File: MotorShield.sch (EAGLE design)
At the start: 88 parts, among them IC1 OPA4340E, IC2 OPA4340E

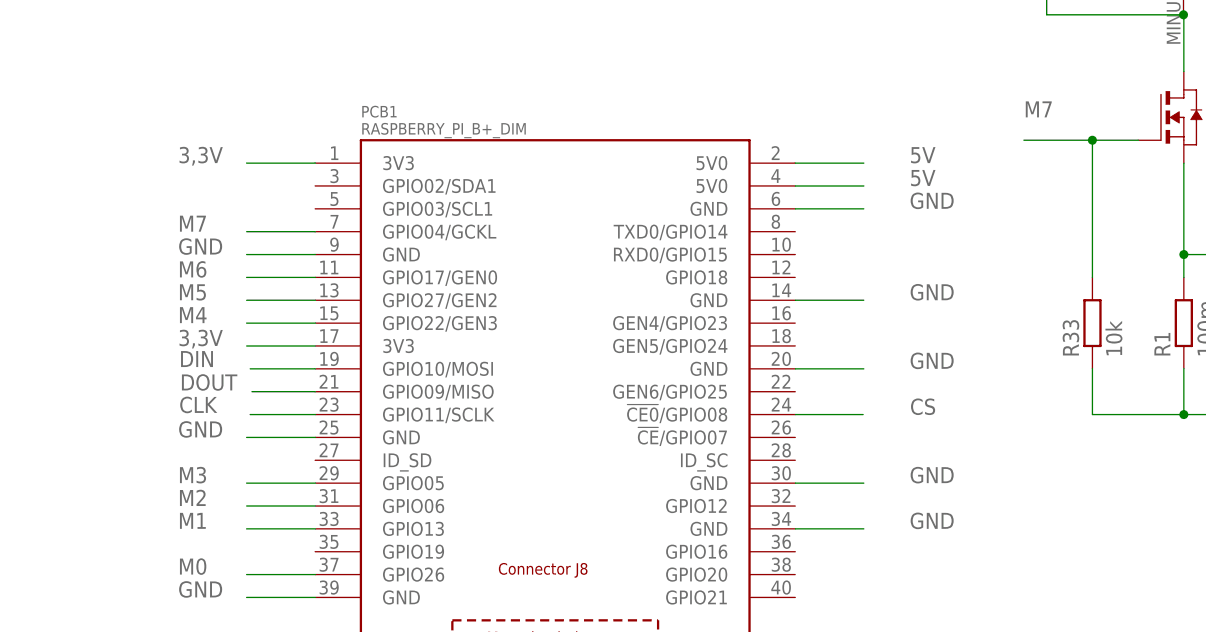
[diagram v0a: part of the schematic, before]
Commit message: marked gpios that are used by s.usv basic, see #10
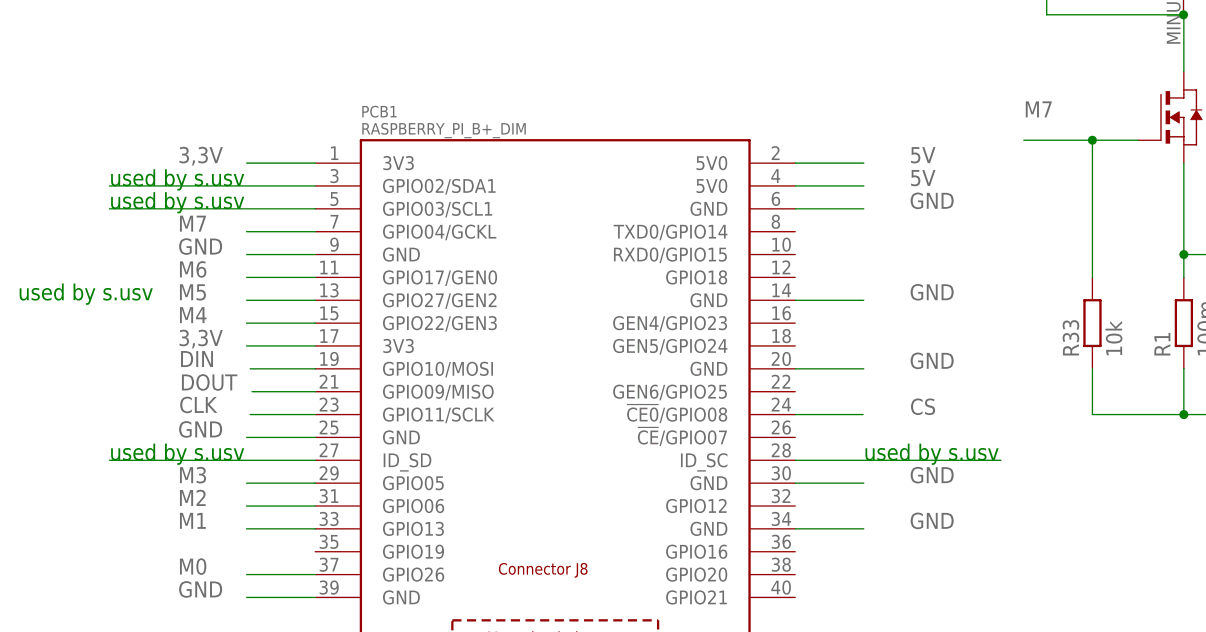
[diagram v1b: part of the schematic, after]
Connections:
- new net N$16: PCB1.GPIO02/SDA1
- new net N$19: PCB1.ID_SD
- new net N$20: PCB1.ID_SC
- new net N$21: PCB1.GPIO03/SCL1
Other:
- note added: "used by s.usv"
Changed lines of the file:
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@@
 <?xml version="1.0" encoding="utf-8"?>
 <!DOCTYPE eagle SYSTEM "eagle.dtd">
-<eagle version="8.2.0">
+<eagle version="6.6.0">
 <drawing>
 <settings>
@@
 <sheet>
 <plain>
+<text x="-27.94" y="83.82" size="1.778" layer="91">used by s.usv</text>
+<text x="-27.94" y="81.28" size="1.778" layer="91">used by s.usv</text>
+<text x="-38.1" y="71.12" size="1.778" layer="91">used by s.usv</text>
+<text x="-27.94" y="53.34" size="1.778" layer="91">used by s.usv</text>
+<text x="55.88" y="53.34" size="1.778" layer="91">used by s.usv</text>
 </plain>
 <instances>
@@
 </segment>
 </net>
+<net name="N$16" class="0">
+<segment>
+<pinref part="PCB1" gate="G$1" pin="GPIO02/SDA1"/>
+<wire x1="-5.08" y1="83.82" x2="-27.94" y2="83.82" width="0.1524" layer="91"/>
+</segment>
+</net>
+<net name="N$19" class="0">
+<segment>
+<pinref part="PCB1" gate="G$1" pin="ID_SD"/>
+<wire x1="-5.08" y1="53.34" x2="-27.94" y2="53.34" width="0.1524" layer="91"/>
+</segment>
+</net>
+<net name="N$20" class="0">
+<segment>
+<pinref part="PCB1" gate="G$1" pin="ID_SC"/>
+<wire x1="48.26" y1="53.34" x2="71.12" y2="53.34" width="0.1524" layer="91"/>
+</segment>
+</net>
+<net name="N$21" class="0">
+<segment>
+<pinref part="PCB1" gate="G$1" pin="GPIO03/SCL1"/>
+<wire x1="-5.08" y1="81.28" x2="-27.94" y2="81.28" width="0.1524" layer="91"/>
+</segment>
+</net>

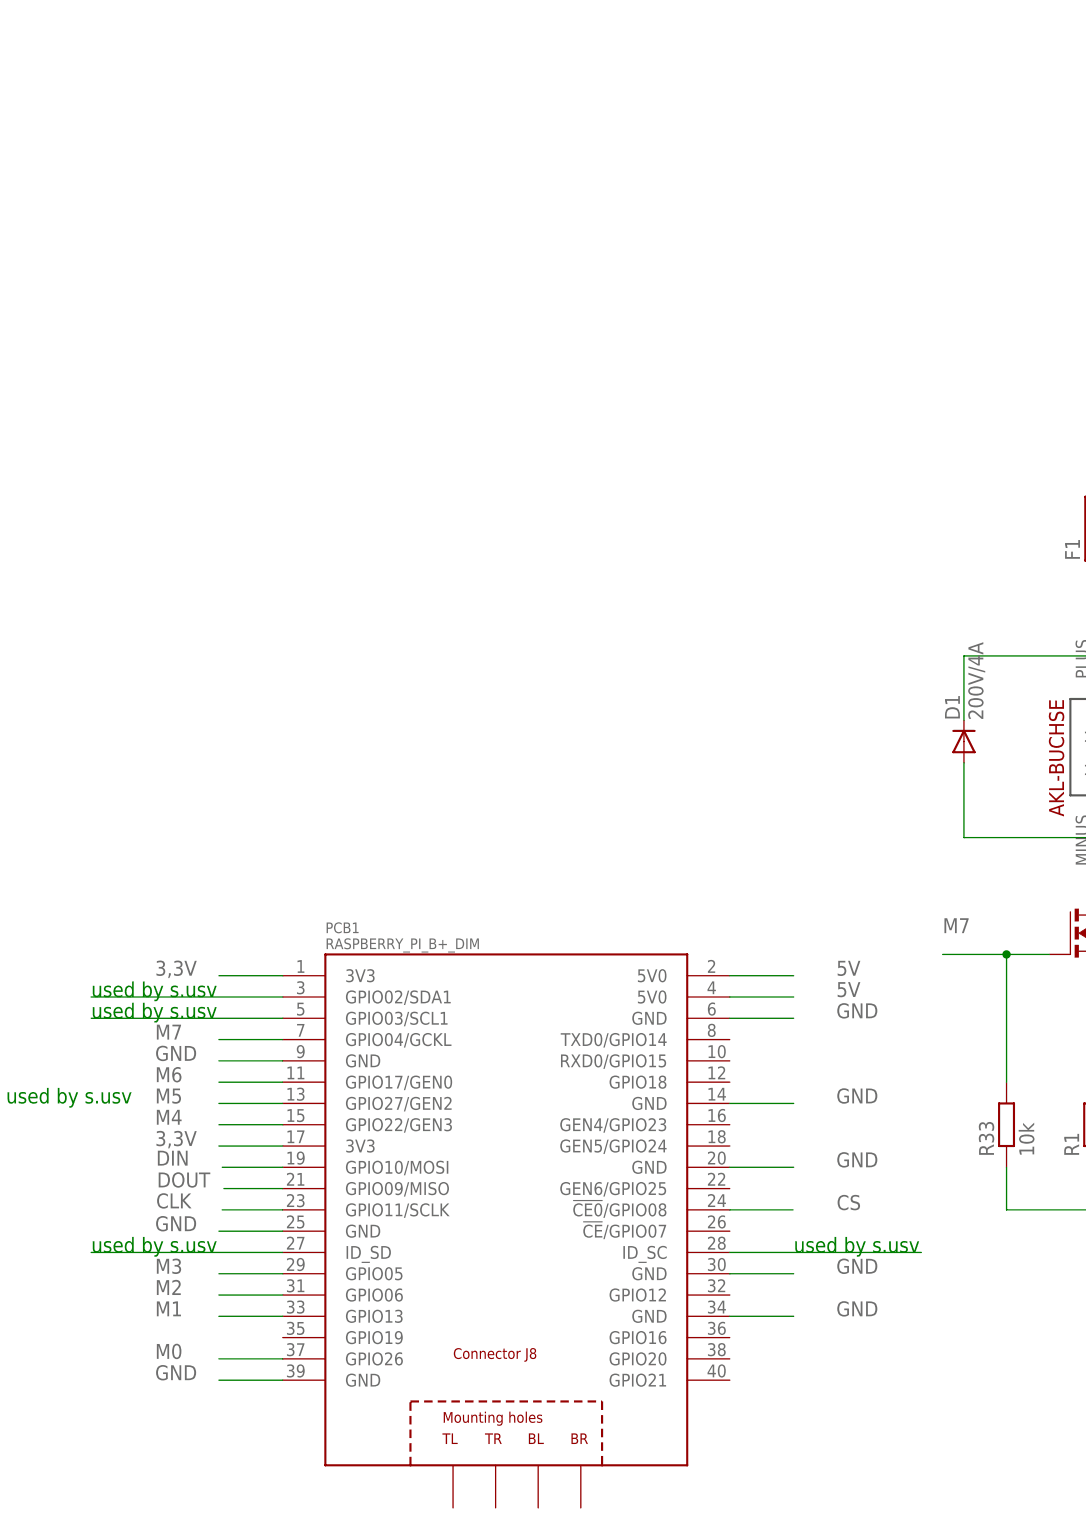
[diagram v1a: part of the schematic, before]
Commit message: added 74HCT125D for DotStar pixels, see #3
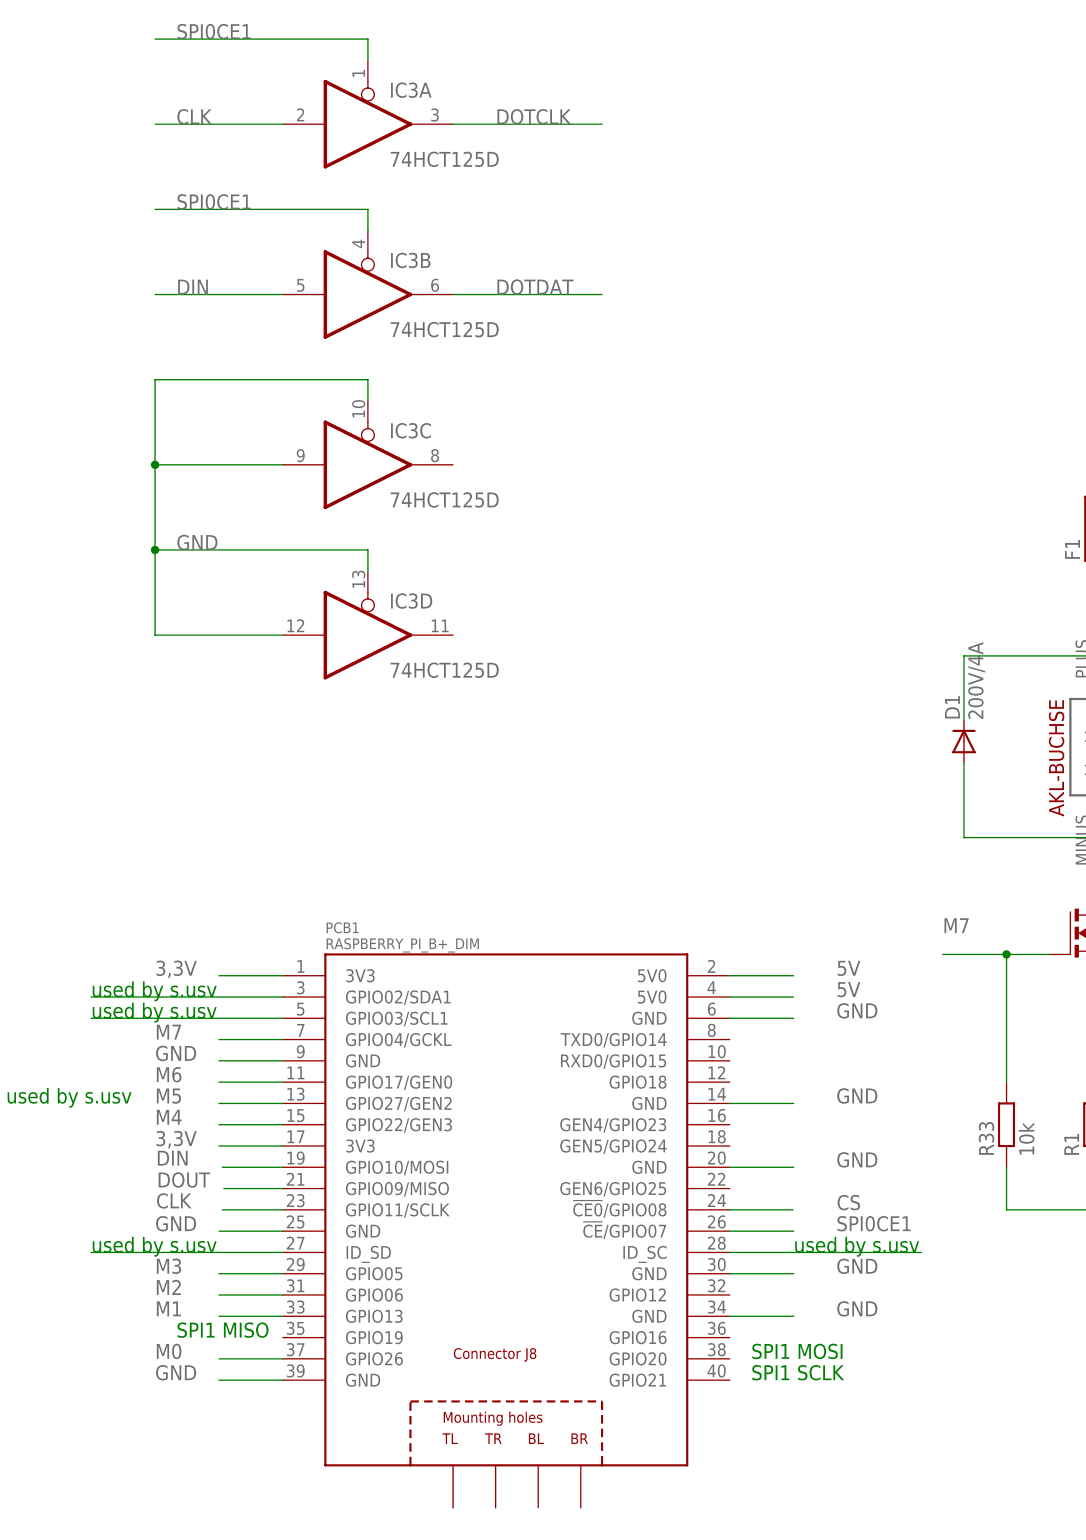
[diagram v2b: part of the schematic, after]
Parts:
- added IC3: 74HCT125D, 74xx-eu:74HCT125D
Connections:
- new net DOTCLK: IC3A.O
- new net DOTDAT: IC3B.O
- new net SPI0CE1: IC3A.OE, IC3B.OE, PCB1.!CE!/GPIO07
- net CLK: now also IC3A.I
- net DIN: now also IC3B.I
- net GND: now also IC3C.I, IC3C.OE, IC3D.I, IC3D.OE
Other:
- note added: "SPI1 MISO"
- note added: "SPI1 MOSI"
- note added: "SPI1 SCLK"
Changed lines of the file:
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@@
 <part name="F8" library="SMD-Fuse" deviceset="POLY-FUSE" device=""/>
 <part name="C10" library="rcl" deviceset="C-EU" device="C1812"/>
+<part name="IC3" library="74xx-eu" deviceset="74*125" device="D" technology="HCT"/>
 </parts>
 <sheets>
@@
 <text x="-27.94" y="53.34" size="1.778" layer="91">used by s.usv</text>
 <text x="55.88" y="53.34" size="1.778" layer="91">used by s.usv</text>
+<text x="50.8" y="38.1" size="1.778" layer="91">SPI1 SCLK</text>
+<text x="50.8" y="40.64" size="1.778" layer="91">SPI1 MOSI</text>
+<text x="-17.78" y="43.18" size="1.778" layer="91">SPI1 MISO</text>
 </plain>
 <instances>
@@
 <instance part="F8" gate="G$1" x="375.92" y="139.7" rot="R90"/>
 <instance part="C10" gate="G$1" x="393.7" y="142.24"/>
+<instance part="IC3" gate="A" x="5.08" y="187.96"/>
+<instance part="IC3" gate="B" x="5.08" y="167.64"/>
+<instance part="IC3" gate="C" x="5.08" y="147.32"/>
+<instance part="IC3" gate="D" x="5.08" y="127"/>
 </instances>
 <busses>
@@
 <label x="-20.32" y="55.88" size="1.778" layer="95"/>
 </segment>
+<segment>
+<pinref part="IC3" gate="C" pin="OE"/>
+<wire x1="5.08" y1="154.94" x2="5.08" y2="157.48" width="0.1524" layer="91"/>
+<wire x1="5.08" y1="157.48" x2="-20.32" y2="157.48" width="0.1524" layer="91"/>
+<pinref part="IC3" gate="D" pin="I"/>
+<wire x1="-20.32" y1="157.48" x2="-20.32" y2="147.32" width="0.1524" layer="91"/>
+<wire x1="-20.32" y1="147.32" x2="-20.32" y2="137.16" width="0.1524" layer="91"/>
+<wire x1="-20.32" y1="137.16" x2="-20.32" y2="127" width="0.1524" layer="91"/>
+<wire x1="-20.32" y1="127" x2="-5.08" y2="127" width="0.1524" layer="91"/>
+<pinref part="IC3" gate="D" pin="OE"/>
+<wire x1="5.08" y1="134.62" x2="5.08" y2="137.16" width="0.1524" layer="91"/>
+<wire x1="5.08" y1="137.16" x2="-20.32" y2="137.16" width="0.1524" layer="91"/>
+<junction x="-20.32" y="137.16"/>
+<pinref part="IC3" gate="C" pin="I"/>
+<wire x1="-5.08" y1="147.32" x2="-20.32" y2="147.32" width="0.1524" layer="91"/>
+<junction x="-20.32" y="147.32"/>
+<label x="-17.78" y="137.16" size="1.778" layer="95"/>
+</segment>
 </net>
 <net name="CH1" class="0">
@@
 <label x="-20.2" y="63.7" size="1.778" layer="95"/>
 </segment>
+<segment>
+<pinref part="IC3" gate="B" pin="I"/>
+<wire x1="-5.08" y1="167.64" x2="-20.32" y2="167.64" width="0.1524" layer="91"/>
+<label x="-17.78" y="167.64" size="1.778" layer="95"/>
+</segment>
 </net>
 <net name="DOUT" class="0">
@@
 <wire x1="-5.08" y1="58.42" x2="-12.3" y2="58.42" width="0.1524" layer="91"/>
 <label x="-20.2" y="58.6" size="1.778" layer="95"/>
+</segment>
+<segment>
+<pinref part="IC3" gate="A" pin="I"/>
+<wire x1="-5.08" y1="187.96" x2="-20.32" y2="187.96" width="0.1524" layer="91"/>
+<label x="-17.78" y="187.96" size="1.778" layer="95"/>
 </segment>
 </net>
@@
 </segment>
 </net>
+<net name="DOTCLK" class="0">
+<segment>
+<pinref part="IC3" gate="A" pin="O"/>
+<wire x1="15.24" y1="187.96" x2="33.02" y2="187.96" width="0.1524" layer="91"/>
+<label x="20.32" y="187.96" size="1.778" layer="95"/>
+</segment>
+</net>
+<net name="DOTDAT" class="0">
+<segment>
+<pinref part="IC3" gate="B" pin="O"/>
+<wire x1="15.24" y1="167.64" x2="33.02" y2="167.64" width="0.1524" layer="91"/>
+<label x="20.32" y="167.64" size="1.778" layer="95"/>
+</segment>
+</net>
+<net name="SPI0CE1" class="0">
+<segment>
+<pinref part="PCB1" gate="G$1" pin="!CE!/GPIO07"/>
+<wire x1="48.26" y1="55.88" x2="55.88" y2="55.88" width="0.1524" layer="91"/>
+<label x="60.96" y="55.88" size="1.778" layer="95"/>
+</segment>
+<segment>
+<pinref part="IC3" gate="B" pin="OE"/>
+<wire x1="5.08" y1="175.26" x2="5.08" y2="177.8" width="0.1524" layer="91"/>
+<wire x1="5.08" y1="177.8" x2="-20.32" y2="177.8" width="0.1524" layer="91"/>
+<label x="-17.78" y="177.8" size="1.778" layer="95"/>
+</segment>
+<segment>
+<pinref part="IC3" gate="A" pin="OE"/>
+<wire x1="5.08" y1="195.58" x2="5.08" y2="198.12" width="0.1524" layer="91"/>
+<wire x1="5.08" y1="198.12" x2="-20.32" y2="198.12" width="0.1524" layer="91"/>
+<label x="-17.78" y="198.12" size="1.778" layer="95"/>
+</segment>
+</net>

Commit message: pump no. 5 is now controlled by GPIO23 fixes #10
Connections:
- net CS renamed CS_ADC
- new net CS_DOTSTARS: PCB1.!CE!/GPIO07
- new net GPIO27: PCB1.GPIO27/GEN2
- net M5: now also PCB1.GEN4/GPIO23; no longer PCB1.GPIO27/GEN2
- net SPI0CE1: no longer PCB1.!CE!/GPIO07
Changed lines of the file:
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@@
 <text x="-27.94" y="83.82" size="1.778" layer="91">used by s.usv</text>
 <text x="-27.94" y="81.28" size="1.778" layer="91">used by s.usv</text>
-<text x="-38.1" y="71.12" size="1.778" layer="91">used by s.usv</text>
+<text x="-27.94" y="71.12" size="1.778" layer="91">used by s.usv</text>
 <text x="-27.94" y="53.34" size="1.778" layer="91">used by s.usv</text>
 <text x="55.88" y="53.34" size="1.778" layer="91">used by s.usv</text>
@@
 </segment>
 <segment>
-<pinref part="PCB1" gate="G$1" pin="GPIO27/GEN2"/>
-<wire x1="-5.08" y1="71.12" x2="-12.7" y2="71.12" width="0.1524" layer="91"/>
-<label x="-20.32" y="71.12" size="1.778" layer="95"/>
+<pinref part="PCB1" gate="G$1" pin="GEN4/GPIO23"/>
+<wire x1="48.26" y1="68.58" x2="55.88" y2="68.58" width="0.1524" layer="91"/>
+<label x="60.96" y="68.58" size="1.778" layer="95"/>
 </segment>
 </net>
@@
 </segment>
 </net>
-<net name="CS" class="0">
+<net name="CS_ADC" class="0">
 <segment>
 <pinref part="U$58" gate="G$1" pin="CS/SHDN"/>
@@
 <net name="SPI0CE1" class="0">
 <segment>
-<pinref part="PCB1" gate="G$1" pin="!CE!/GPIO07"/>
-<wire x1="48.26" y1="55.88" x2="55.88" y2="55.88" width="0.1524" layer="91"/>
-<label x="60.96" y="55.88" size="1.778" layer="95"/>
-</segment>
-<segment>
 <pinref part="IC3" gate="B" pin="OE"/>
 <wire x1="5.08" y1="175.26" x2="5.08" y2="177.8" width="0.1524" layer="91"/>
@@
 </segment>
 </net>
+<net name="CS_DOTSTARS" class="0">
+<segment>
+<pinref part="PCB1" gate="G$1" pin="!CE!/GPIO07"/>
+<wire x1="48.26" y1="55.88" x2="55.88" y2="55.88" width="0.1524" layer="91"/>
+<label x="60.96" y="55.88" size="1.778" layer="95"/>
+</segment>
+</net>
+<net name="GPIO27" class="0">
+<segment>
+<pinref part="PCB1" gate="G$1" pin="GPIO27/GEN2"/>
+<wire x1="-5.08" y1="71.12" x2="-12.7" y2="71.12" width="0.1524" layer="91"/>
+</segment>
+</net>
